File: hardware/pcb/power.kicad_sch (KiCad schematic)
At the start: 59 parts, among them Q1 EPC2305, Q2 EPC2305, U1 LMR36520FADDAR, U2 LMG1210RVRT, U3 LP5907MFX-3.3/NOPB, U5 OPA333AIDBVR, U6 INA241A2QDGKRQ1

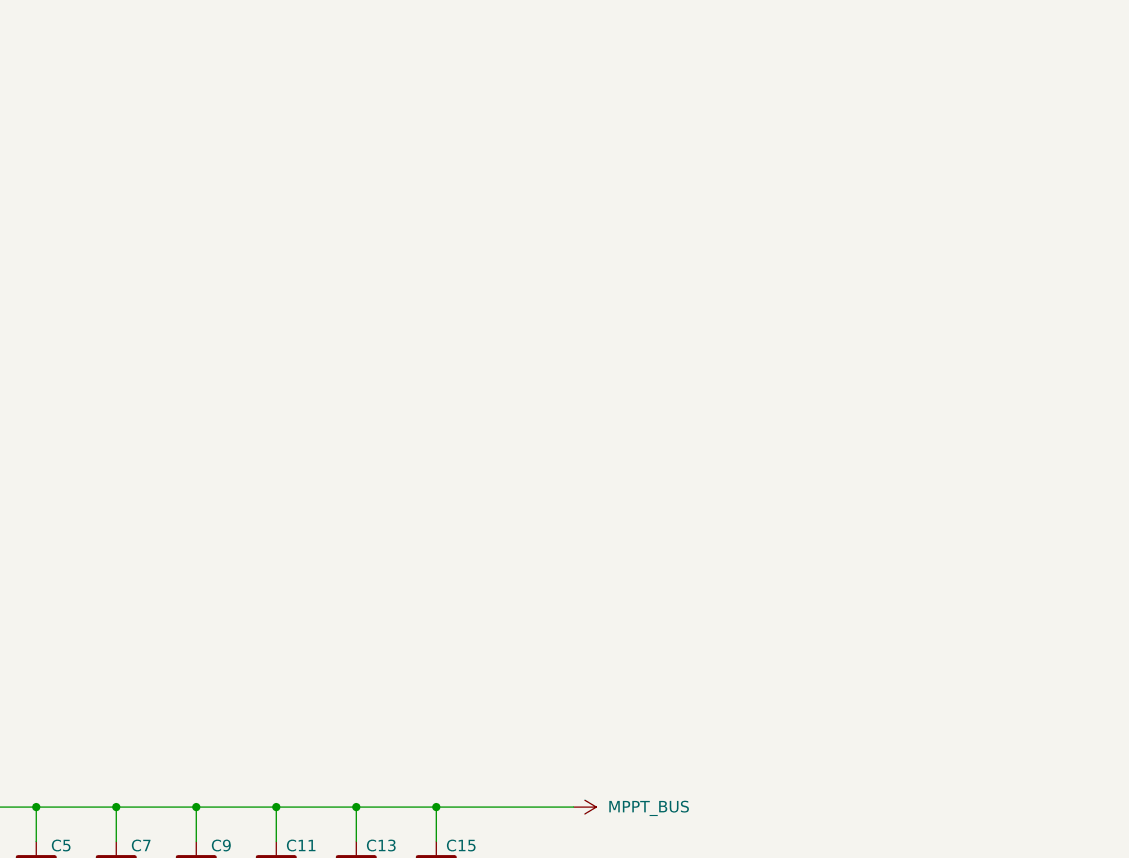
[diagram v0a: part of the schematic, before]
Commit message: Add TPS48110 disconnect, OVP, and discharge design; update MCU and power schematics
Documents the buck high-side short-circuit fault, programmable output
overvoltage protection, and controlled output discharge, and records the
saved schematic changes.

Co-Authored-By: Claude Opus 5.5 <noreply@anthropic.com>
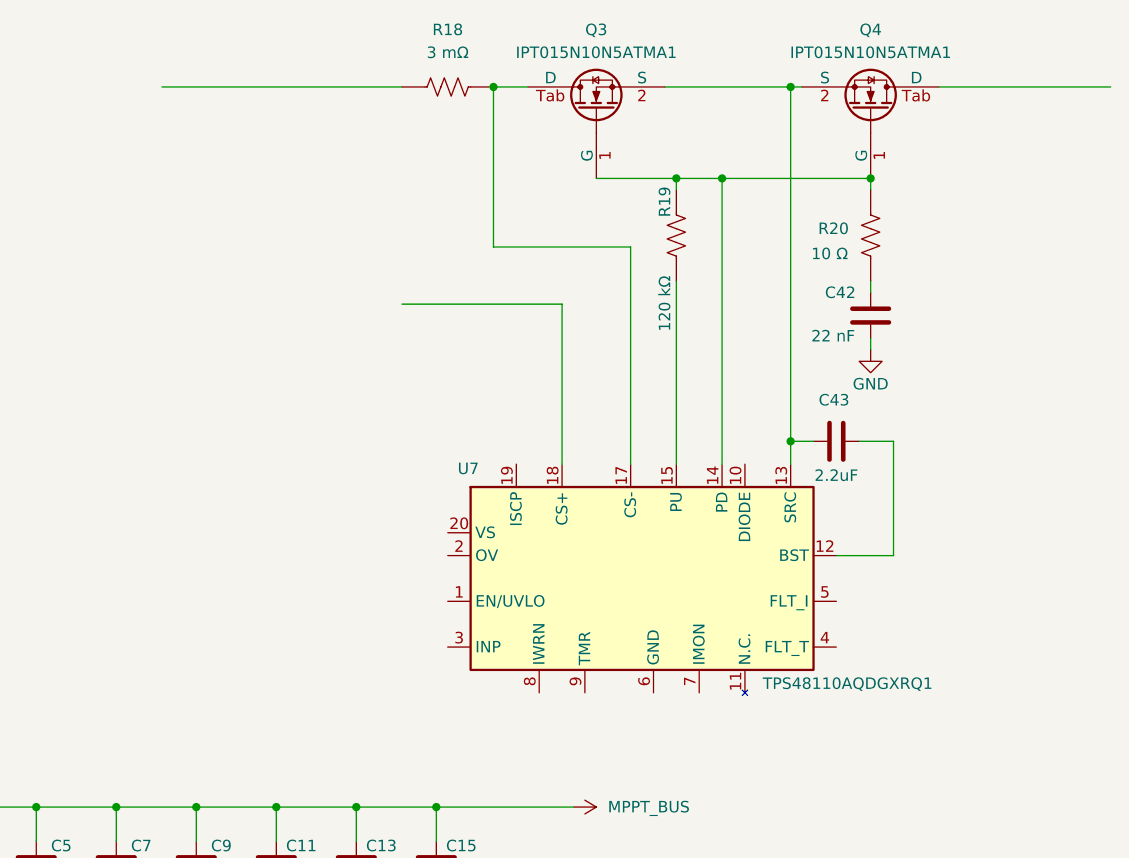
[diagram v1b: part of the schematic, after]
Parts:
- added C42: 22 nF, verified:C_0805_2012Metric, symbol verified:CGA4J1C0G2A223J125AC
- added C43: 2.2uF, verified:C_1210_3225Metric, symbol verified:GRM32ER72A225KA35L
- added Q3, Q4: IPT015N10N5ATMA1, verified:IPT015N10N5ATMA1_PCB, symbol verified:IPT015N10N5ATMA1
- added R18: 3 mΩ, verified:R_2512_6332Metric, symbol verified:CSNL2512FT3L00
- added R19: 120 kΩ, verified:R_0402_1005Metric, symbol verified:RC0402FR-07120KL
- added R20: 10 Ω, verified:R_0805_2012Metric, symbol verified:RCA080510R0FKEAHP
- added U7: TPS48110AQDGXRQ1, verified:TPS48110AQDGXRQ1_PCB, symbol verified:TPS48110AQDGXRQ1
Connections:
- net GND: now also C42.2
- new net: Q3.Tab (D), R18.2, U7.17 (CS-)
- new net: Q3.1 (G), Q4.1 (G), R19.1, R20.1, U7.14 (PD)
- new net: C43.1, Q3.2 (S), Q3.3 (S), Q3.4 (S), Q3.5 (S), Q3.6 (S), Q3.7 (S), Q3.8 (S), Q4.2 (S), Q4.3 (S), Q4.4 (S), Q4.5 (S), Q4.6 (S), Q4.7 (S), Q4.8 (S), U7.13 (SRC)
- new net: C42.1, R20.2
- new net: C43.2, U7.12 (BST)
- new net: R19.2, U7.15 (PU)
